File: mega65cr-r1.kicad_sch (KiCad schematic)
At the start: 19 parts, among them J13 Conn_01x04_Male, J14 Conn_02x17_Odd_Even, J16 Conn_01x04_Male, U1 74HC245, U2 74HC245, U3 74HC245

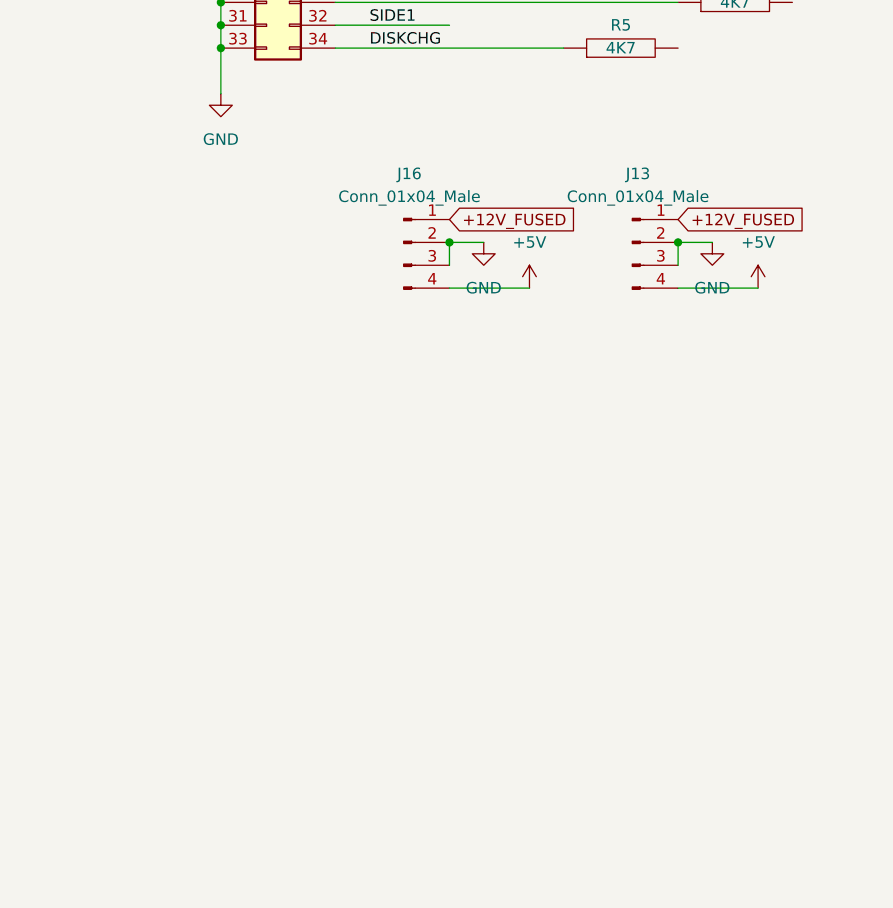
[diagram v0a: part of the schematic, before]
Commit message: add IEC port connector and footprint
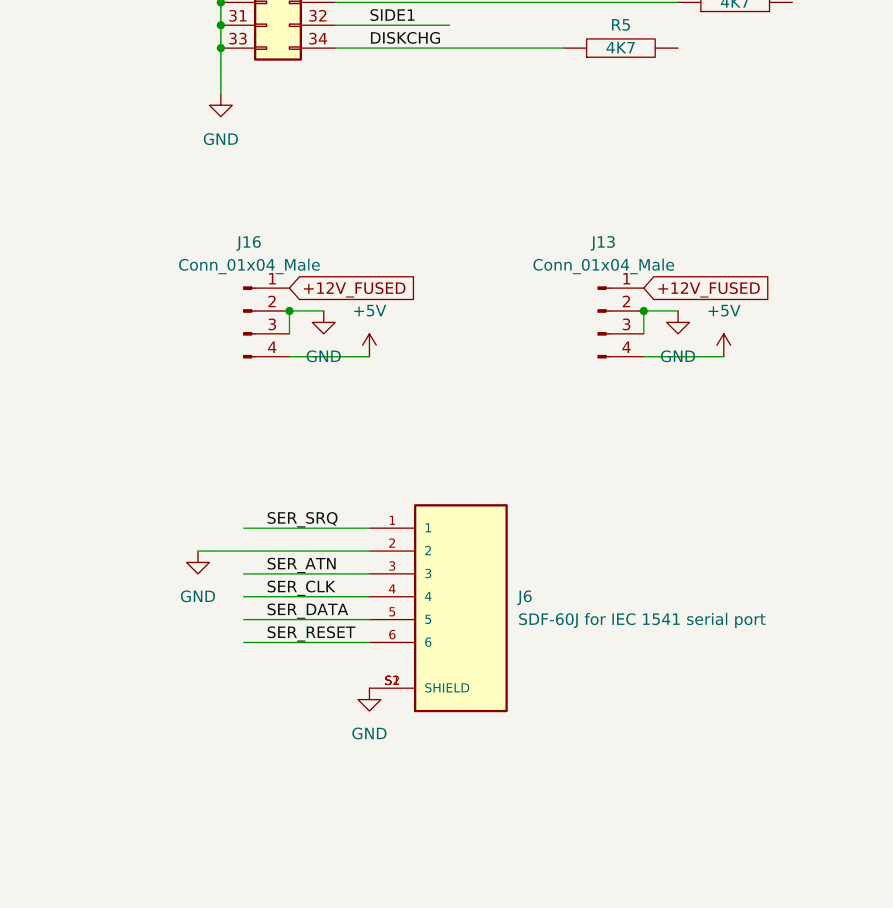
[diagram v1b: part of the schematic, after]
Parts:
- added J6: SDF-60J for IEC 1541 serial port, CUI_SDF-60J, symbol snapeda:SDF-60J
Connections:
- net GND: now also J6.2, J6.S1 (SHIELD), J6.S2 (SHIELD)
- new net SER_ATN: J6.3
- new net SER_CLK: J6.4
- new net SER_DATA: J6.5
- new net SER_RESET: J6.6
- new net SER_SRQ: J6.1
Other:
- moved on the sheet: J13, J16

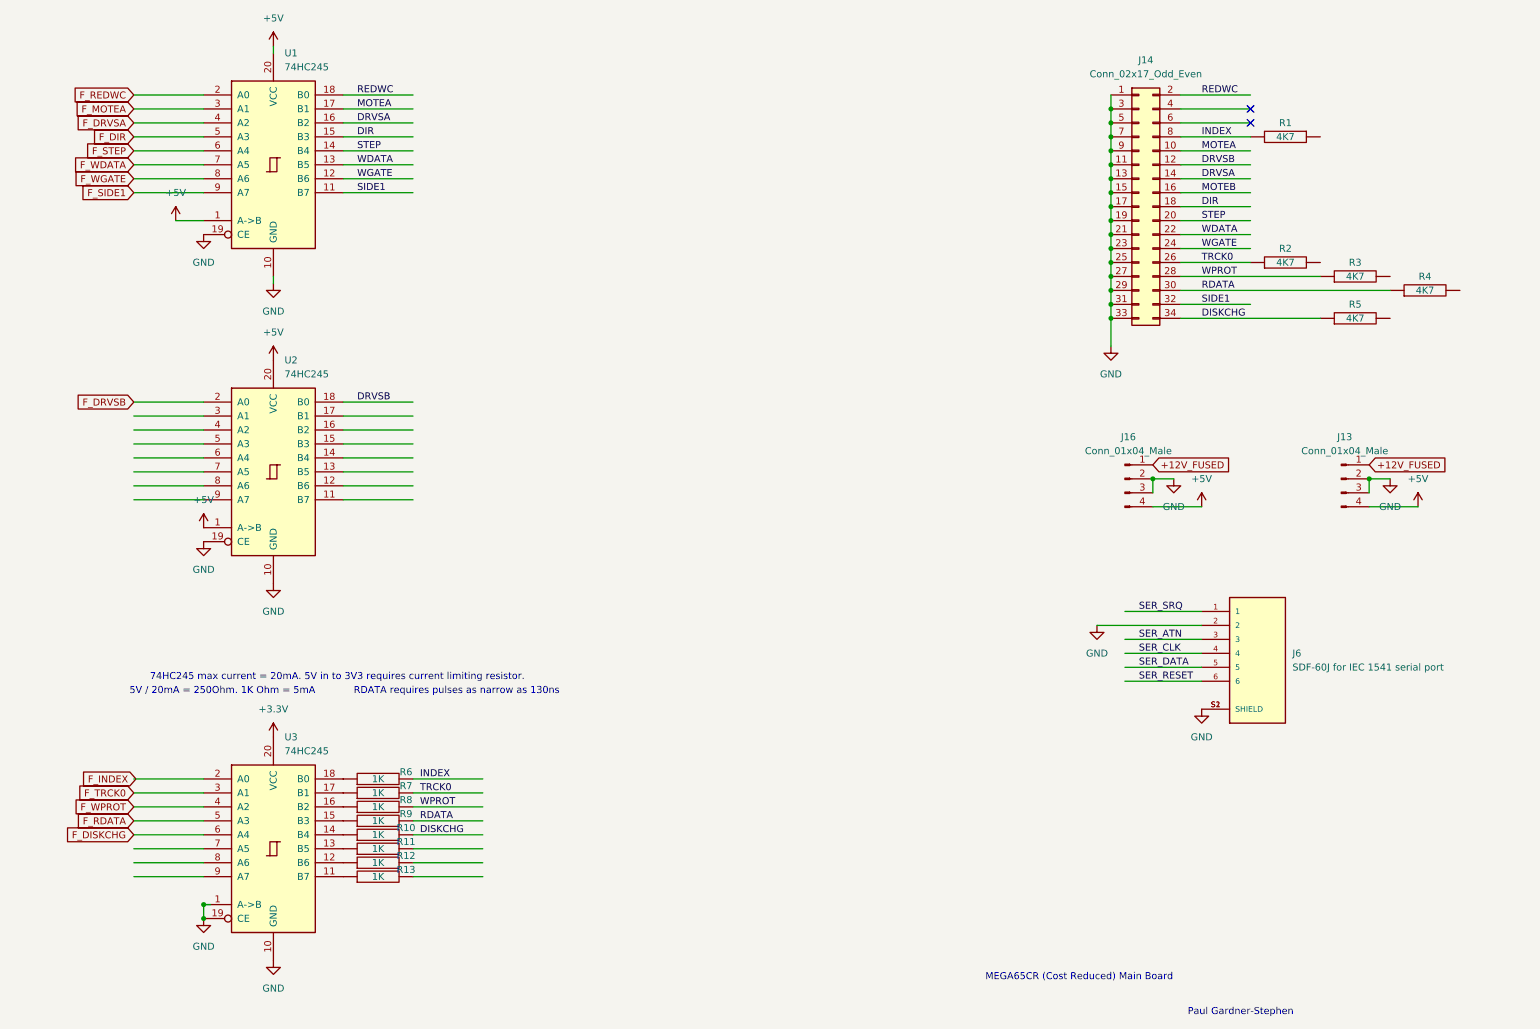
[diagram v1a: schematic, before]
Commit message: complete IEC and 34-pin floppy interface sheet
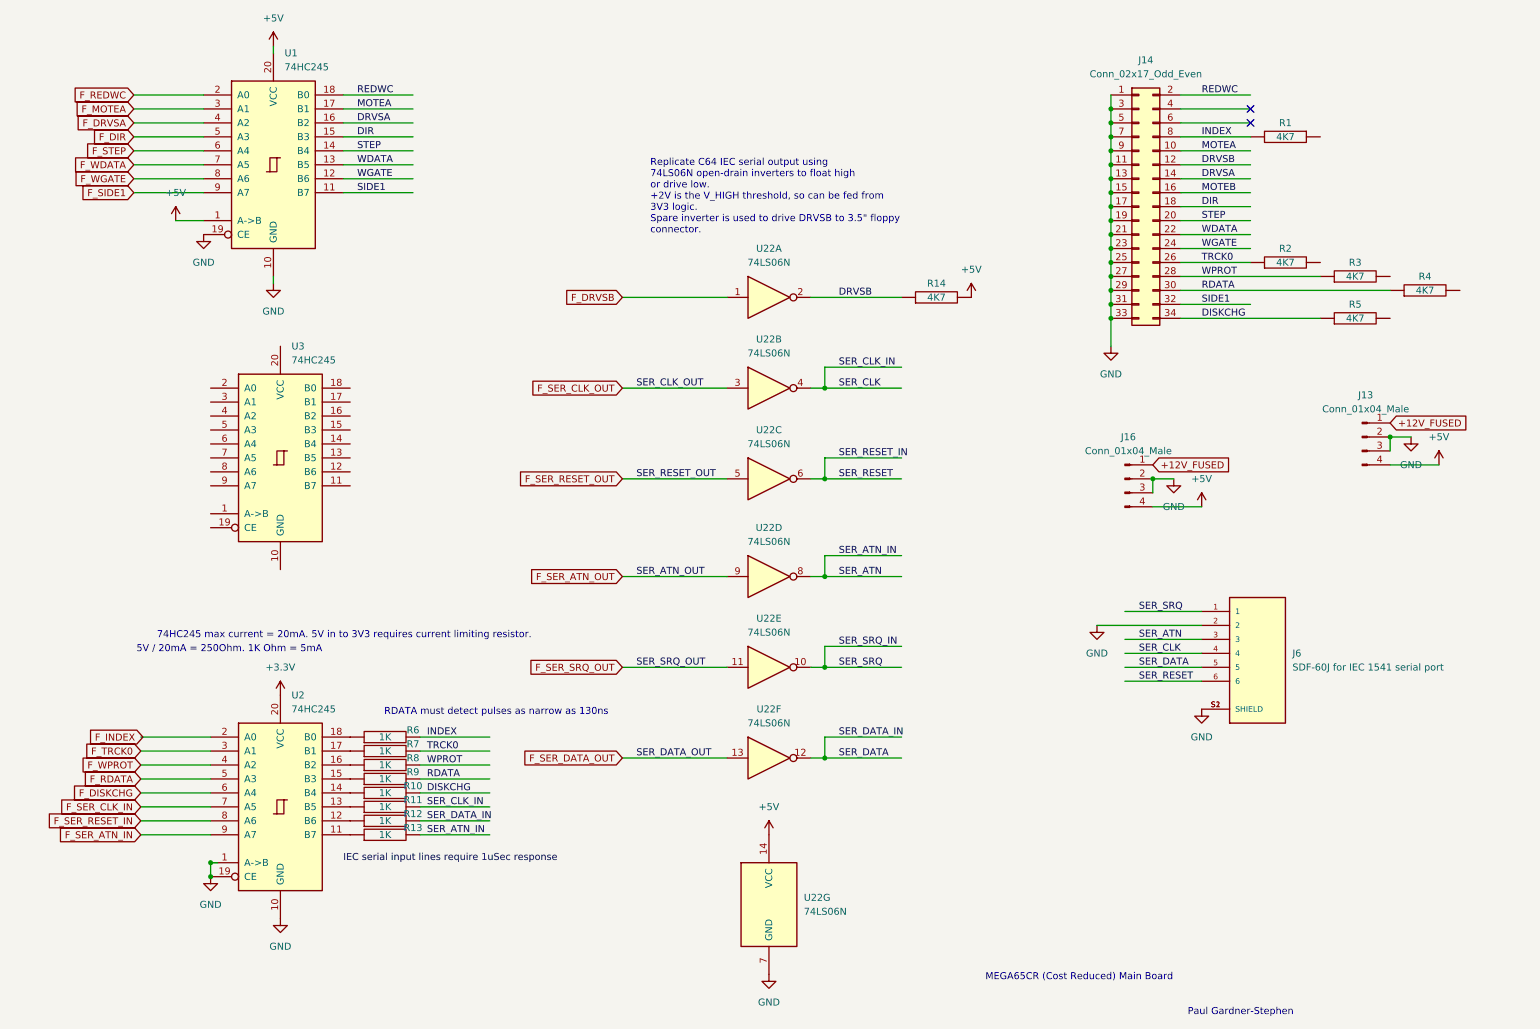
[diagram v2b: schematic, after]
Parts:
- removed U2: 74HC245, symbol 74xx:74HC245
- added R14: 4K7, Resistor_THT:R_Box_L8.4mm_W2.5mm_P5.08mm, symbol pspice:R
- added U22: 74LS06N, Package_DIP:DIP-14_W7.62mm, symbol 74xx:74LS06N
- added U3: 74HC245, Package_DIP:DIP-20_W7.62mm, symbol 74xx:74HC245
- J13, J16: footprint (none) -> PinHeader_1x04_P2.54mm_Vertical
- J14: footprint (none) -> Connector_PinHeader_2.54mm:PinHeader_2x17_P2.54mm_Vertical
- R1, R10, R11, R12, R13, R2, R3, R4, R5, R6, R7, R8, R9: footprint (none) -> Resistor_THT:R_Box_L8.4mm_W2.5mm_P5.08mm
- U2: renamed from U3; footprint (none) -> Package_DIP:DIP-20_W7.62mm
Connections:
- net +5V: now also R14.2, U22.14 (VCC)
- net DRVSB: now also R14.1, U22.2
- net F_DRVSB: now also U22.1
- net GND: now also U22.7 (GND)
- net SER_ATN: now also R13.2, U22.8
- net SER_CLK: now also R11.2, U22.4
- net SER_DATA: now also R12.2, U22.12
- net SER_RESET: now also U22.6
- net SER_SRQ: now also U22.10
- net F_SER_CLK_IN: now reaches U2.7 (A5)
- net F_SER_RESET_IN: now reaches U2.8 (A6)
- net F_SER_ATN_IN: now reaches U2.9 (A7)
- new net F_SER_ATN_OUT: U22.9
- new net F_SER_CLK_OUT: U22.3
- new net F_SER_DATA_OUT: U22.13
- new net F_SER_RESET_OUT: U22.5
- new net F_SER_SRQ_OUT: U22.11
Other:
- note added: "RDATA must detect pulses as narrow as 130ns"
- note added: "Replicate C64 IEC serial output using 74LS06N open-drain inverters to float high or drive low. +2V is the V_HIGH threshold, so can be fed from 3V3 logic. Spare inverter is used to drive DRVSB to 3.5" floppy connector."
- note removed: "RDATA requires pulses as narrow as 130ns"
- moved on the sheet: J13, R10, R11, R12, R13, R6, R7, R8, R9, U2

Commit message: refactor floppy circuits onto own sheet
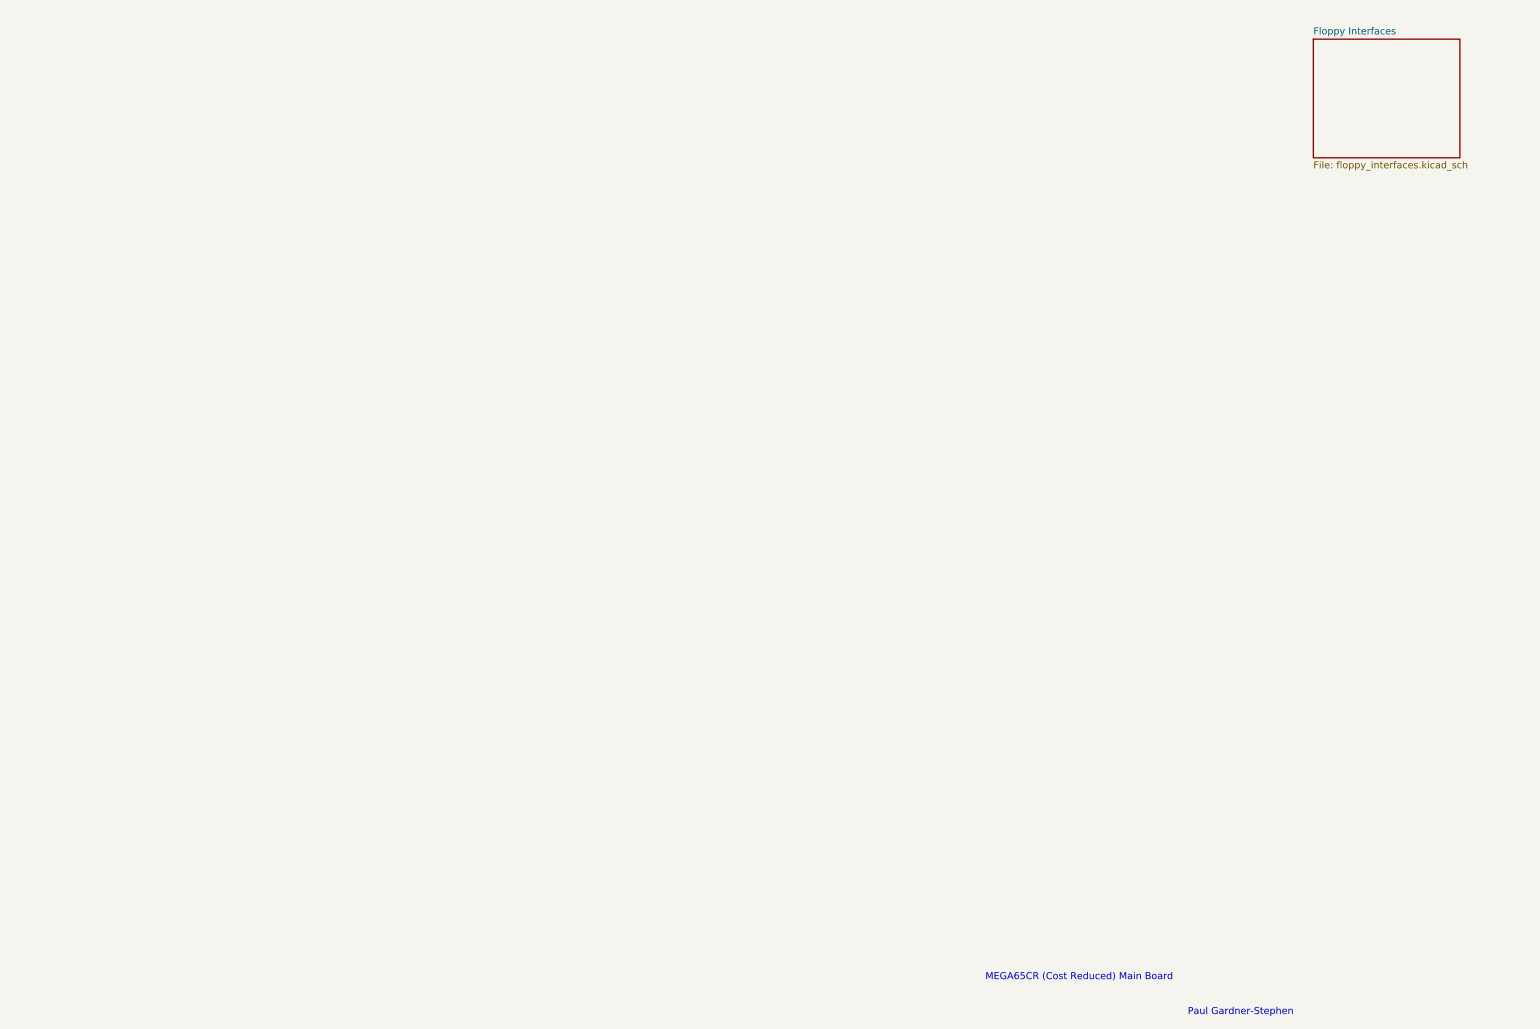
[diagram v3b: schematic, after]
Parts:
- removed J13, J16: Conn_01x04_Male, PinHeader_1x04_P2.54mm_Vertical, symbol Connector:Conn_01x04_Male
- removed J14: Conn_02x17_Odd_Even, Connector_PinHeader_2.54mm:PinHeader_2x17_P2.54mm_Vertical, symbol Connector_Generic:Conn_02x17_Odd_Even
- removed J6: SDF-60J for IEC 1541 serial port, CUI_SDF-60J, symbol snapeda:SDF-60J
- removed R1, R14, R2, R3, R4, R5: 4K7, Resistor_THT:R_Box_L8.4mm_W2.5mm_P5.08mm, symbol pspice:R
- removed R10, R11, R12, R13, R6, R7, R8, R9: 1K, Resistor_THT:R_Box_L8.4mm_W2.5mm_P5.08mm, symbol pspice:R
- removed U1, U2, U3: 74HC245, Package_DIP:DIP-20_W7.62mm, symbol 74xx:74HC245
- removed U22: 74LS06N, Package_DIP:DIP-14_W7.62mm, symbol 74xx:74LS06N
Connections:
- no-connect marks 2 -> 0
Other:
- added sheet Floppy Interfaces (floppy_interfaces.kicad_sch)
- note removed: "5V / 20mA = 250Ohm. 1K Ohm = 5mA"
- note removed: "74HC245 max current = 20mA. 5V in to 3V3 requires current limiting resistor."
- note removed: "RDATA must detect pulses as narrow as 130ns"
- note removed: "Replicate C64 IEC serial output using 74LS06N open-drain inverters to float high or drive low. +2V is the V_HIGH threshold, so can be fed from 3V3 logic. Spare inverter is used to drive DRVSB to 3.5" floppy connector."

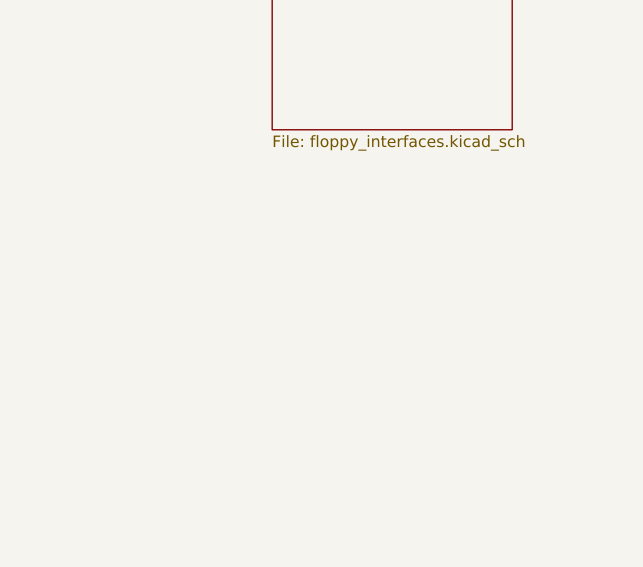
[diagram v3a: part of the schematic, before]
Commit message: add joystick sheet
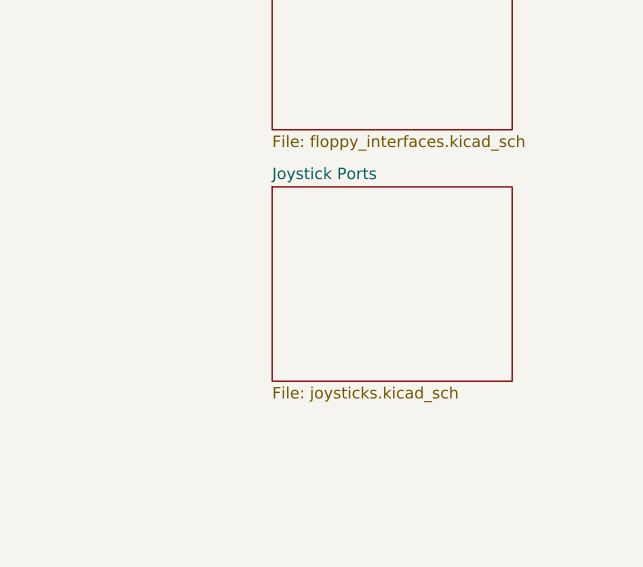
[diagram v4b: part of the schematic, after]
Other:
- added sheet Joystick Ports (joysticks.kicad_sch)
